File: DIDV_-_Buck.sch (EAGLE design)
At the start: 33 parts, among them K101 G5LE, Q101 BC817, Q102 BC817, T101 BSC076N06NS3, T102 BSC076N06NS3

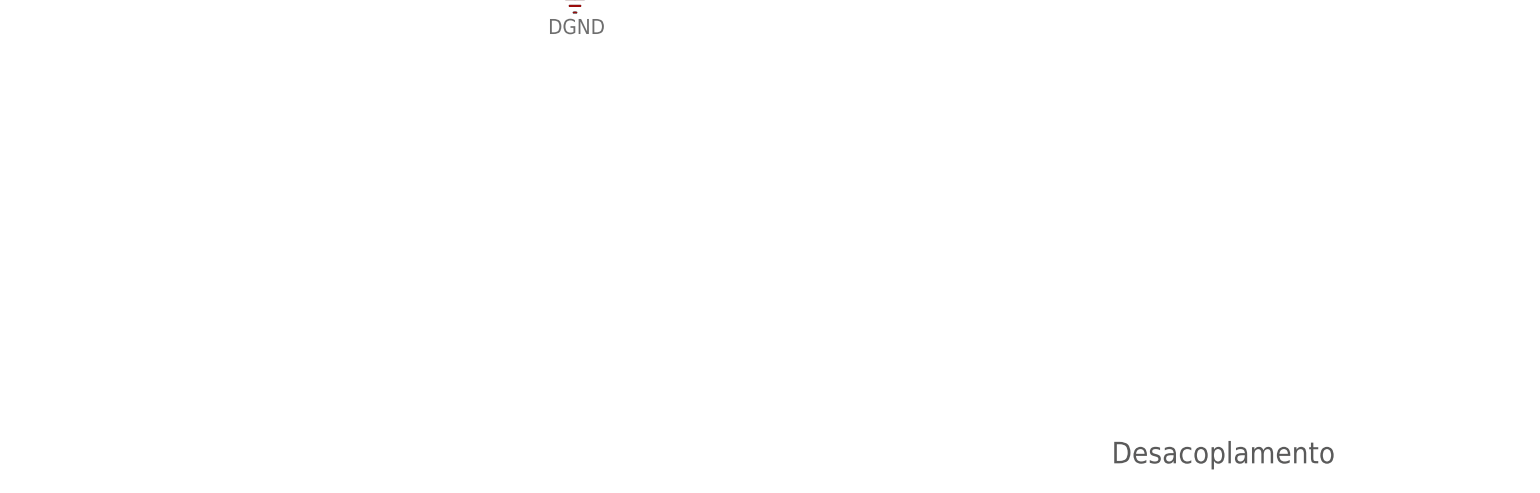
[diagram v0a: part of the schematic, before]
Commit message: Revisão 9
- Corrigidos algumas falhas de ligação
- Implementação com VPRG dos TLCs via Hardware
- Inserção do cálculo do Riref

Obs. Se somente a criação de boards, não será incrementado. No caso, se criado um board novo board vou subir para 9.1 e assim por diante.
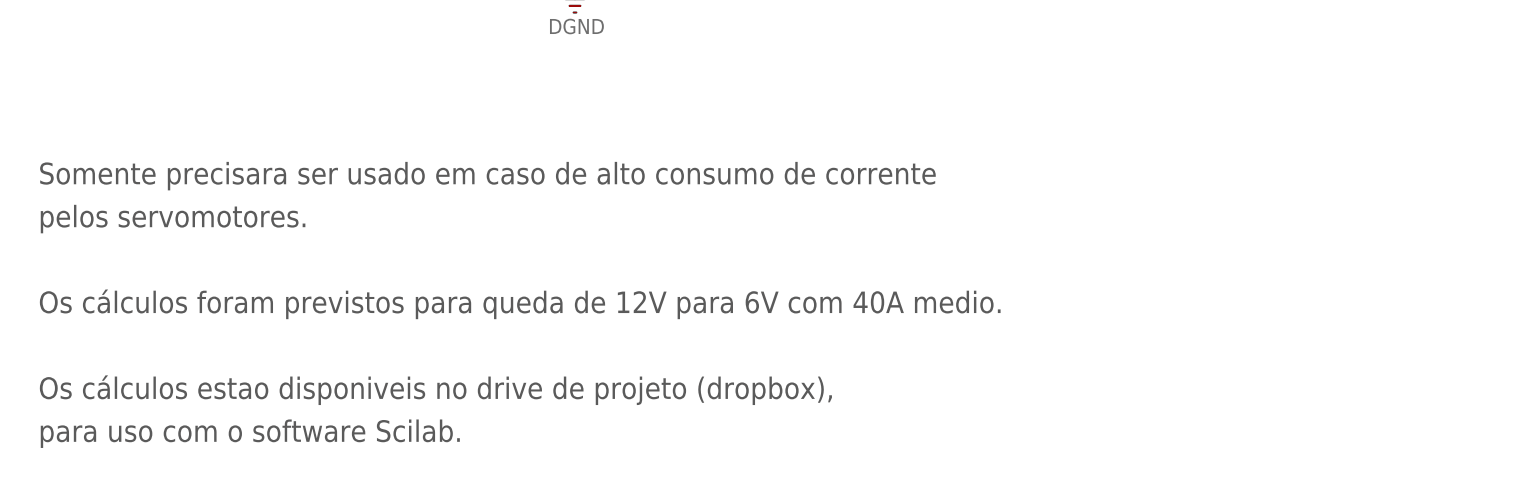
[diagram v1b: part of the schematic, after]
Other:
- note added: "09"
- note added: "Os cálculos estao disponiveis no drive de projeto (dropbox),"
- note added: "Os cálculos foram previstos para queda de 12V para 6V com 40A medio."
- note added: "Somente precisara ser usado em caso de alto consumo de corrente"
- note added: "para uso com o software Scilab."
- note added: "pelos servomotores."
- note removed: "08"
- note removed: "Desacoplamento"
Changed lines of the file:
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@@
 <text x="203.2" y="29.464" size="1.778" layer="150" font="vector">Dispositivo de Interface para</text>
 <text x="210.82" y="26.162" size="1.778" layer="150" font="vector">Deficientes Visuais</text>
-<text x="250.698" y="10.16" size="2.54" layer="150" font="vector">08</text>
-<text x="134.62" y="10.16" size="2.54" layer="97" font="vector">Desacoplamento</text>
+<text x="250.698" y="10.16" size="2.54" layer="150" font="vector">09</text>
+<text x="7.62" y="43.18" size="2.54" layer="97" font="vector">Somente precisara ser usado em caso de alto consumo de corrente</text>
+<text x="7.62" y="38.1" size="2.54" layer="97" font="vector">pelos servomotores.</text>
+<text x="7.62" y="27.94" size="2.54" layer="97" font="vector">Os cálculos foram previstos para queda de 12V para 6V com 40A medio.</text>
+<text x="7.62" y="17.78" size="2.54" layer="97" font="vector">Os cálculos estao disponiveis no drive de projeto (dropbox),</text>
+<text x="7.62" y="12.7" size="2.54" layer="97" font="vector">para uso com o software Scilab.</text>
 </plain>
 <instances>
